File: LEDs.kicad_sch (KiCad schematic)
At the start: 13 parts

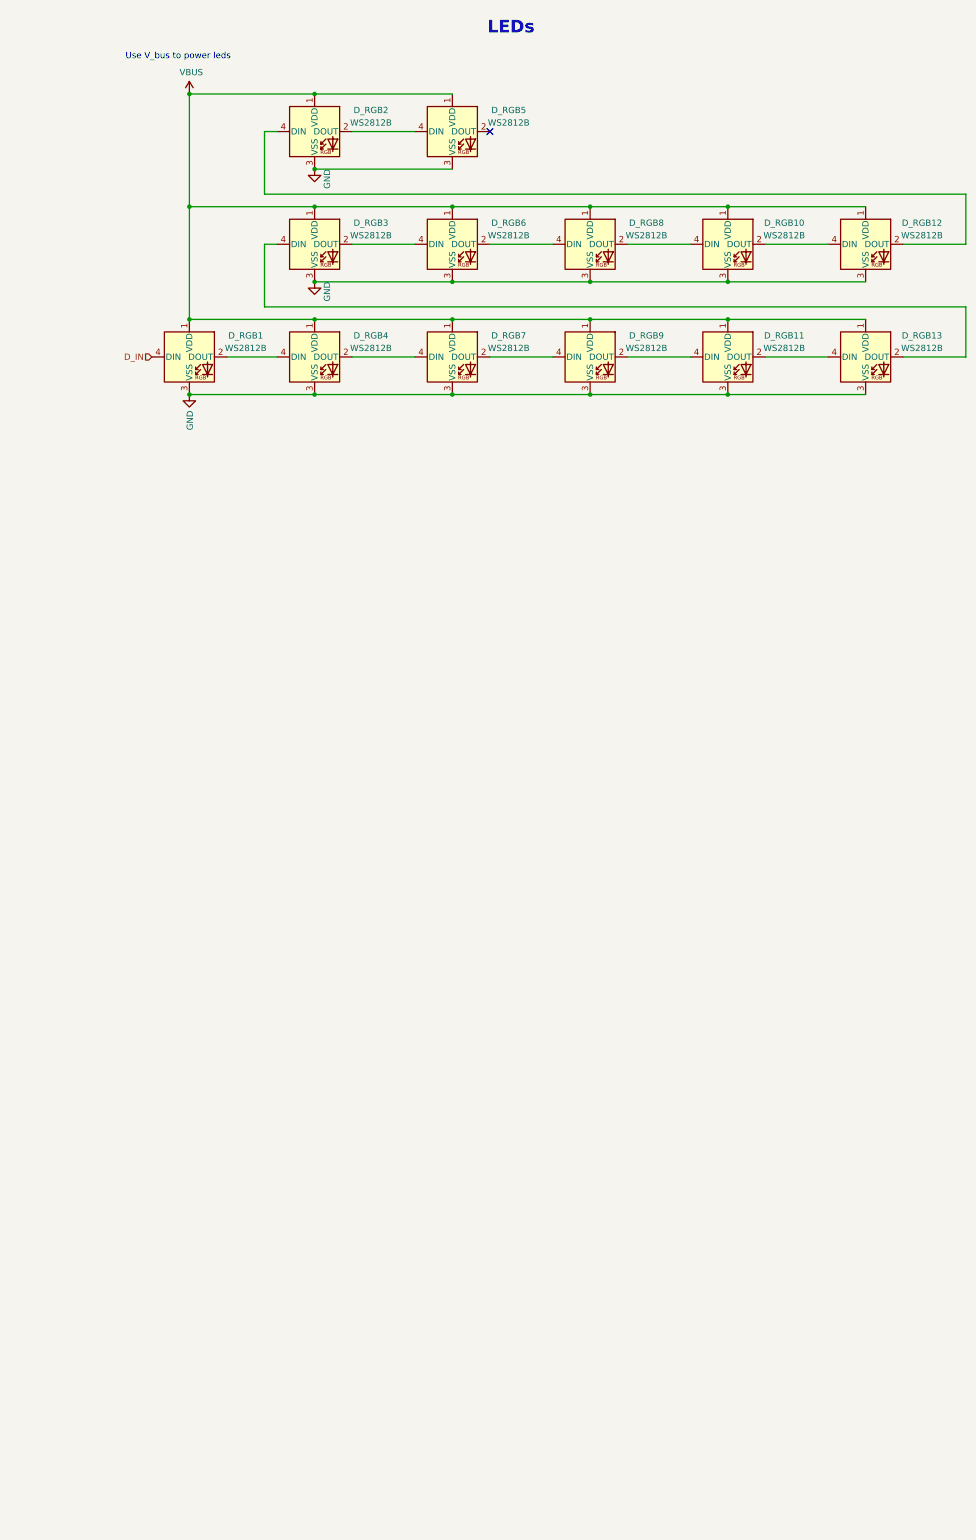
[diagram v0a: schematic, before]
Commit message: per key rgb (reverse mount sk6812 mini e, geometry finalisation
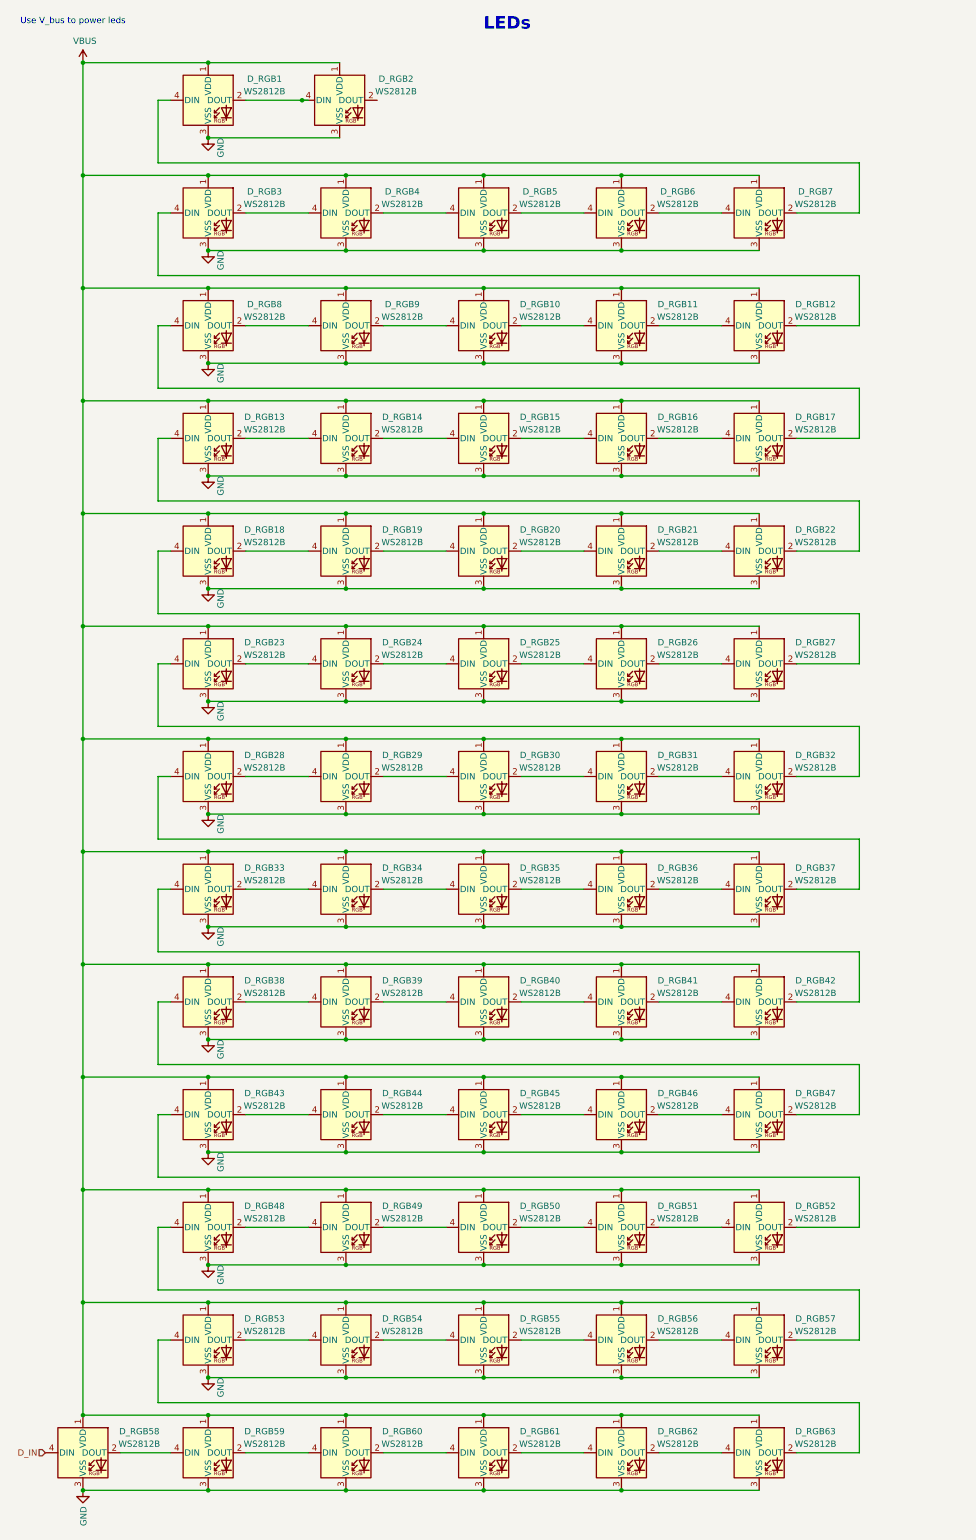
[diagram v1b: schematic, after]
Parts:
- added D_RGB1, D_RGB10, D_RGB11, D_RGB12, D_RGB13, D_RGB14, D_RGB15, D_RGB16, D_RGB17, D_RGB18, D_RGB19, D_RGB20, D_RGB21, D_RGB22, D_RGB23, D_RGB24, D_RGB25, D_RGB26, D_RGB27, D_RGB28, D_RGB29, D_RGB3, D_RGB30, D_RGB31, D_RGB32, D_RGB33, D_RGB34, D_RGB35, D_RGB36, D_RGB37, D_RGB38, D_RGB39, D_RGB4, D_RGB40, D_RGB41, D_RGB42, D_RGB43, D_RGB44, D_RGB45, D_RGB46, D_RGB47, D_RGB48, D_RGB49, D_RGB50, D_RGB51, D_RGB52, D_RGB6, D_RGB7, D_RGB8, D_RGB9: WS2812B, kbd:LED_SK6812MINI_E_3.5x3.5mm_P1.75mm, symbol LED:WS2812B
- D_RGB2, D_RGB5: footprint LED_SMD:LED_WS2812B_PLCC4_5.0x5.0mm_P3.2mm -> kbd:LED_SK6812MINI_E_3.5x3.5mm_P1.75mm
- D_RGB53: renamed from D_RGB3; footprint LED_SMD:LED_WS2812B_PLCC4_5.0x5.0mm_P3.2mm -> kbd:LED_SK6812MINI_E_3.5x3.5mm_P1.75mm
- D_RGB54: renamed from D_RGB6; footprint LED_SMD:LED_WS2812B_PLCC4_5.0x5.0mm_P3.2mm -> kbd:LED_SK6812MINI_E_3.5x3.5mm_P1.75mm
- D_RGB55: renamed from D_RGB8; footprint LED_SMD:LED_WS2812B_PLCC4_5.0x5.0mm_P3.2mm -> kbd:LED_SK6812MINI_E_3.5x3.5mm_P1.75mm
- D_RGB56: renamed from D_RGB10; footprint LED_SMD:LED_WS2812B_PLCC4_5.0x5.0mm_P3.2mm -> kbd:LED_SK6812MINI_E_3.5x3.5mm_P1.75mm
- D_RGB57: renamed from D_RGB12; footprint LED_SMD:LED_WS2812B_PLCC4_5.0x5.0mm_P3.2mm -> kbd:LED_SK6812MINI_E_3.5x3.5mm_P1.75mm
- D_RGB58: renamed from D_RGB1; footprint Connector_JST:JST_XH_B5B-XH-A_1x05_P2.50mm_Vertical -> kbd:LED_SK6812MINI_E_3.5x3.5mm_P1.75mm
- D_RGB59: renamed from D_RGB4; footprint LED_SMD:LED_WS2812B_PLCC4_5.0x5.0mm_P3.2mm -> kbd:LED_SK6812MINI_E_3.5x3.5mm_P1.75mm
- D_RGB60: renamed from D_RGB7; footprint LED_SMD:LED_WS2812B_PLCC4_5.0x5.0mm_P3.2mm -> kbd:LED_SK6812MINI_E_3.5x3.5mm_P1.75mm
- D_RGB61: renamed from D_RGB9; footprint LED_SMD:LED_WS2812B_PLCC4_5.0x5.0mm_P3.2mm -> kbd:LED_SK6812MINI_E_3.5x3.5mm_P1.75mm
- D_RGB62: renamed from D_RGB11; footprint LED_SMD:LED_WS2812B_PLCC4_5.0x5.0mm_P3.2mm -> kbd:LED_SK6812MINI_E_3.5x3.5mm_P1.75mm
- D_RGB63: renamed from D_RGB13; footprint LED_SMD:LED_WS2812B_PLCC4_5.0x5.0mm_P3.2mm -> kbd:LED_SK6812MINI_E_3.5x3.5mm_P1.75mm
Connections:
- net GND: now also D_RGB1.3 (VSS), D_RGB10.3 (VSS), D_RGB11.3 (VSS), D_RGB12.3 (VSS), D_RGB13.3 (VSS), D_RGB14.3 (VSS), D_RGB15.3 (VSS), D_RGB16.3 (VSS), D_RGB17.3 (VSS), D_RGB18.3 (VSS), D_RGB19.3 (VSS), D_RGB20.3 (VSS), D_RGB21.3 (VSS), D_RGB22.3 (VSS), D_RGB23.3 (VSS), D_RGB24.3 (VSS), D_RGB25.3 (VSS), D_RGB26.3 (VSS), D_RGB27.3 (VSS), D_RGB28.3 (VSS), D_RGB29.3 (VSS), D_RGB3.3 (VSS), D_RGB30.3 (VSS), D_RGB31.3 (VSS), D_RGB32.3 (VSS), D_RGB33.3 (VSS), D_RGB34.3 (VSS), D_RGB35.3 (VSS), D_RGB36.3 (VSS), D_RGB37.3 (VSS), D_RGB38.3 (VSS), D_RGB39.3 (VSS), D_RGB4.3 (VSS), D_RGB40.3 (VSS), D_RGB41.3 (VSS), D_RGB42.3 (VSS), D_RGB43.3 (VSS), D_RGB44.3 (VSS), D_RGB45.3 (VSS), D_RGB46.3 (VSS), D_RGB47.3 (VSS), D_RGB48.3 (VSS), D_RGB49.3 (VSS), D_RGB50.3 (VSS), D_RGB51.3 (VSS), D_RGB52.3 (VSS), D_RGB6.3 (VSS), D_RGB7.3 (VSS), D_RGB8.3 (VSS), D_RGB9.3 (VSS)
- net VBUS: now also D_RGB1.1 (VDD), D_RGB10.1 (VDD), D_RGB11.1 (VDD), D_RGB12.1 (VDD), D_RGB13.1 (VDD), D_RGB14.1 (VDD), D_RGB15.1 (VDD), D_RGB16.1 (VDD), D_RGB17.1 (VDD), D_RGB18.1 (VDD), D_RGB19.1 (VDD), D_RGB20.1 (VDD), D_RGB21.1 (VDD), D_RGB22.1 (VDD), D_RGB23.1 (VDD), D_RGB24.1 (VDD), D_RGB25.1 (VDD), D_RGB26.1 (VDD), D_RGB27.1 (VDD), D_RGB28.1 (VDD), D_RGB29.1 (VDD), D_RGB3.1 (VDD), D_RGB30.1 (VDD), D_RGB31.1 (VDD), D_RGB32.1 (VDD), D_RGB33.1 (VDD), D_RGB34.1 (VDD), D_RGB35.1 (VDD), D_RGB36.1 (VDD), D_RGB37.1 (VDD), D_RGB38.1 (VDD), D_RGB39.1 (VDD), D_RGB4.1 (VDD), D_RGB40.1 (VDD), D_RGB41.1 (VDD), D_RGB42.1 (VDD), D_RGB43.1 (VDD), D_RGB44.1 (VDD), D_RGB45.1 (VDD), D_RGB46.1 (VDD), D_RGB47.1 (VDD), D_RGB48.1 (VDD), D_RGB49.1 (VDD), D_RGB50.1 (VDD), D_RGB51.1 (VDD), D_RGB52.1 (VDD), D_RGB6.1 (VDD), D_RGB7.1 (VDD), D_RGB8.1 (VDD), D_RGB9.1 (VDD)
- net at D_RGB2.4 (DIN): now also D_RGB1.2 (DOUT); no longer D_RGB57.2 (DOUT)
- net at D_RGB5.4 (DIN): now also D_RGB4.2 (DOUT); no longer D_RGB2.2 (DOUT)
- net at D_RGB5.2 (DOUT): now also D_RGB6.4 (DIN)
- new net: D_RGB13.2 (DOUT), D_RGB14.4 (DIN)
- new net: D_RGB13.4 (DIN), D_RGB22.2 (DOUT)
- new net: D_RGB18.2 (DOUT), D_RGB19.4 (DIN)
- new net: D_RGB18.4 (DIN), D_RGB27.2 (DOUT)
- new net: D_RGB51.2 (DOUT), D_RGB52.4 (DIN)
- new net: D_RGB50.2 (DOUT), D_RGB51.4 (DIN)
- new net: D_RGB44.2 (DOUT), D_RGB45.4 (DIN)
- new net: D_RGB43.2 (DOUT), D_RGB44.4 (DIN)
- new net: D_RGB41.2 (DOUT), D_RGB42.4 (DIN)
- new net: D_RGB40.2 (DOUT), D_RGB41.4 (DIN)
- new net: D_RGB28.2 (DOUT), D_RGB29.4 (DIN)
- new net: D_RGB28.4 (DIN), D_RGB37.2 (DOUT)
- new net: D_RGB14.2 (DOUT), D_RGB15.4 (DIN)
- new net: D_RGB33.2 (DOUT), D_RGB34.4 (DIN)
- new net: D_RGB33.4 (DIN), D_RGB42.2 (DOUT)
- new net: D_RGB3.2 (DOUT), D_RGB4.4 (DIN)
- new net: D_RGB31.2 (DOUT), D_RGB32.4 (DIN)
- new net: D_RGB30.2 (DOUT), D_RGB31.4 (DIN)
- new net: D_RGB16.2 (DOUT), D_RGB17.4 (DIN)
- new net: D_RGB15.2 (DOUT), D_RGB16.4 (DIN)
- new net: D_RGB10.2 (DOUT), D_RGB11.4 (DIN)
- new net: D_RGB10.4 (DIN), D_RGB9.2 (DOUT)
- new net: D_RGB11.2 (DOUT), D_RGB12.4 (DIN)
- new net: D_RGB45.2 (DOUT), D_RGB46.4 (DIN)
- new net: D_RGB36.2 (DOUT), D_RGB37.4 (DIN)
- new net: D_RGB46.2 (DOUT), D_RGB47.4 (DIN)
- new net: D_RGB23.2 (DOUT), D_RGB24.4 (DIN)
- new net: D_RGB23.4 (DIN), D_RGB32.2 (DOUT)
- new net: D_RGB8.2 (DOUT), D_RGB9.4 (DIN)
- new net: D_RGB17.2 (DOUT), D_RGB8.4 (DIN)
- new net: D_RGB43.4 (DIN), D_RGB52.2 (DOUT)
- new net: D_RGB38.2 (DOUT), D_RGB39.4 (DIN)
- new net: D_RGB38.4 (DIN), D_RGB47.2 (DOUT)
- new net: D_RGB39.2 (DOUT), D_RGB40.4 (DIN)
- new net: D_RGB48.2 (DOUT), D_RGB49.4 (DIN)
- new net: D_RGB48.4 (DIN), D_RGB57.2 (DOUT)
- new net: D_RGB24.2 (DOUT), D_RGB25.4 (DIN)
- new net: D_RGB26.2 (DOUT), D_RGB27.4 (DIN)
- new net: D_RGB25.2 (DOUT), D_RGB26.4 (DIN)
- new net: D_RGB35.2 (DOUT), D_RGB36.4 (DIN)
- new net: D_RGB12.2 (DOUT), D_RGB3.4 (DIN)
- new net: D_RGB1.4 (DIN), D_RGB7.2 (DOUT)
- new net: D_RGB34.2 (DOUT), D_RGB35.4 (DIN)
- new net: D_RGB6.2 (DOUT), D_RGB7.4 (DIN)
- new net: D_RGB29.2 (DOUT), D_RGB30.4 (DIN)
- new net: D_RGB19.2 (DOUT), D_RGB20.4 (DIN)
- new net: D_RGB20.2 (DOUT), D_RGB21.4 (DIN)
- new net: D_RGB21.2 (DOUT), D_RGB22.4 (DIN)
- new net: D_RGB49.2 (DOUT), D_RGB50.4 (DIN)
- no-connect marks 1 -> 0
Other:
- moved on the sheet: D_RGB53, D_RGB54, D_RGB55, D_RGB56, D_RGB57, D_RGB58, D_RGB59, D_RGB60, D_RGB61, D_RGB62, D_RGB63

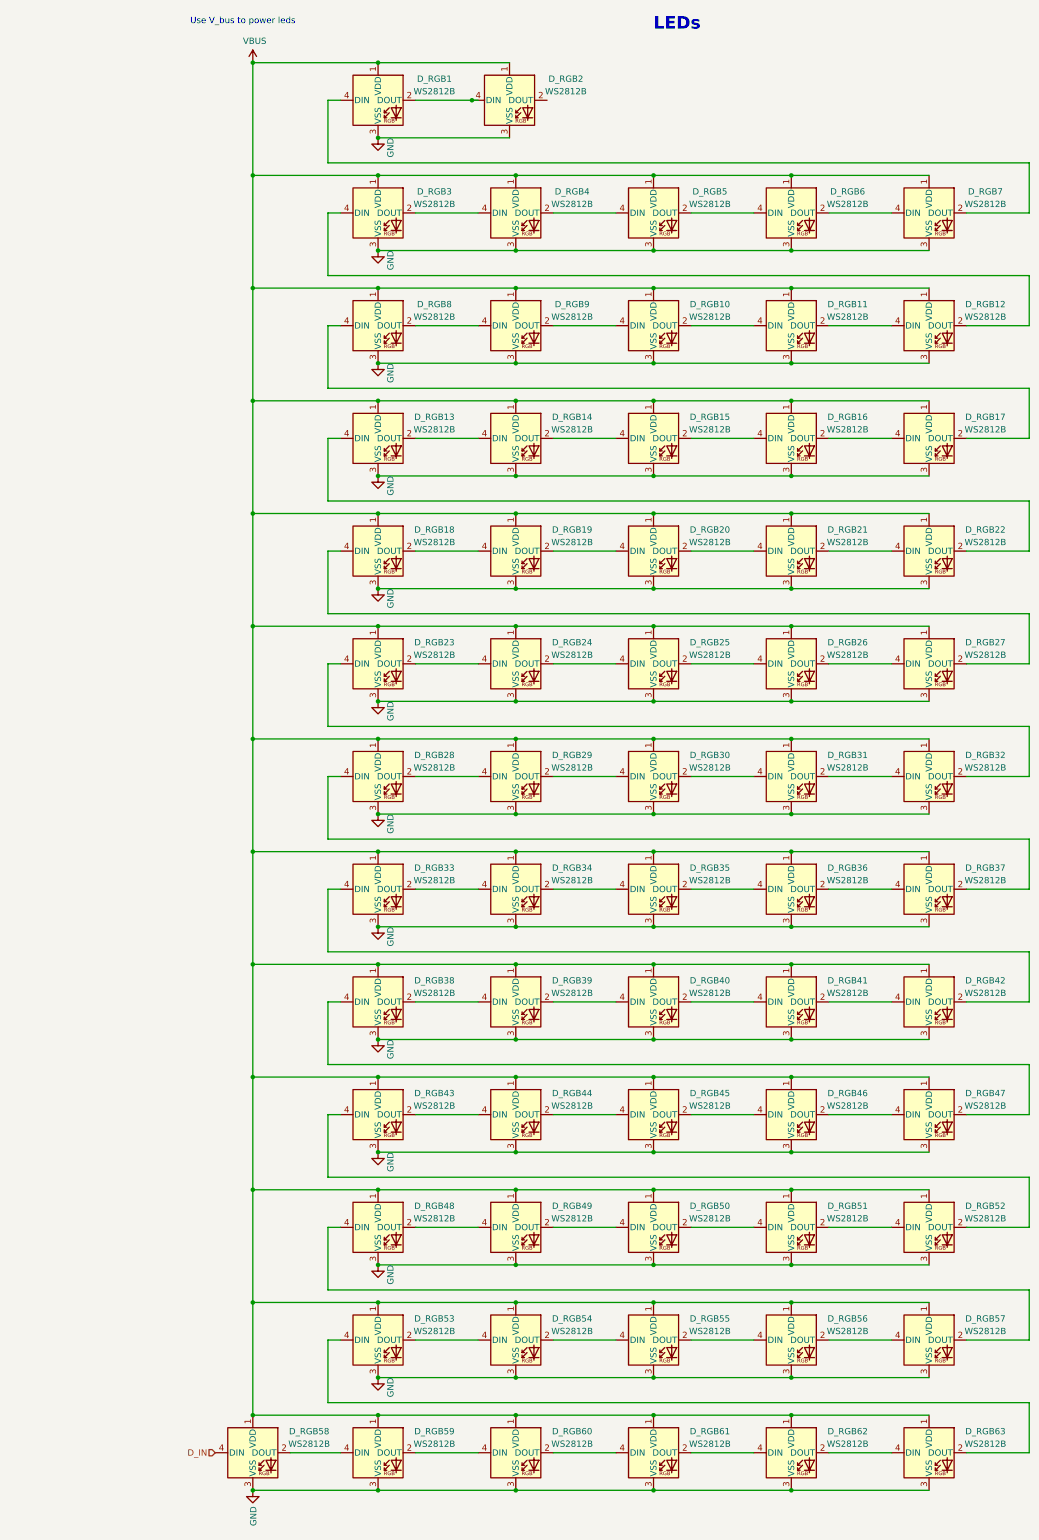
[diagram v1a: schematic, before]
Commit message: remove left most column, reroute rp2040
remove left most column, reroute rp2040 to fit in-between switches, no more oled, last 2 cols (right) are snap off. 
still to do:
- check that the snap cutouts aren't too much,
- add mounting holes for if the side is snapped off.
- still to route columns/rows
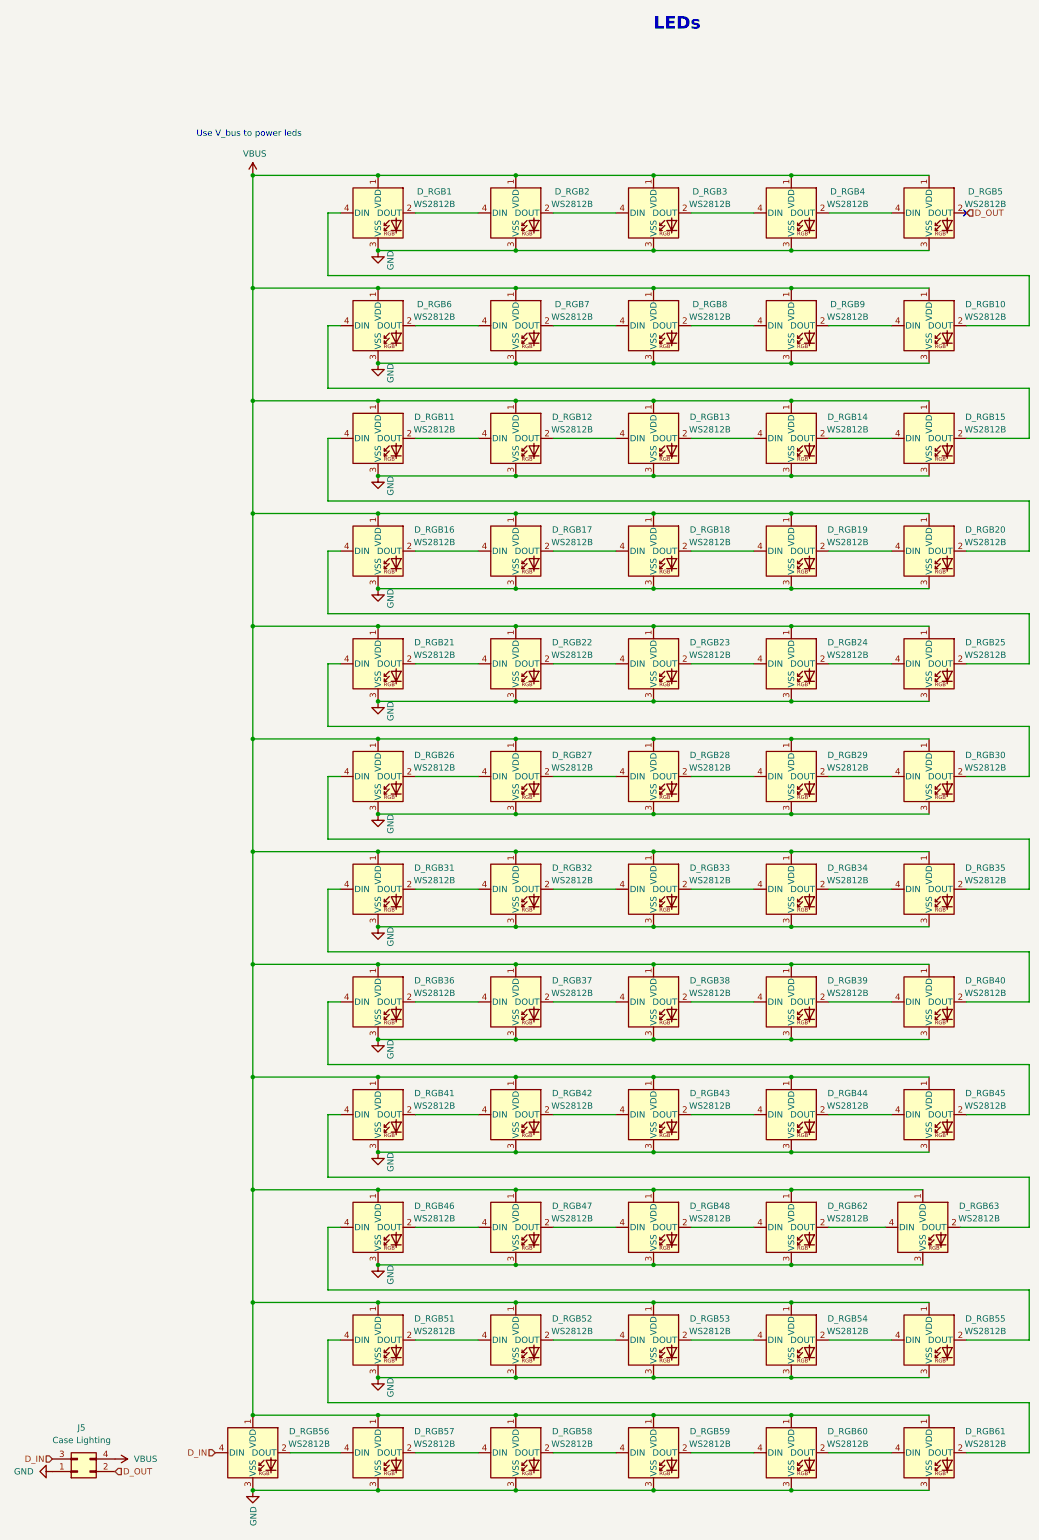
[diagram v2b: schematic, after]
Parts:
- removed D_RGB1, D_RGB2, D_RGB49, D_RGB50, D_RGB52: WS2812B, kbd:LED_SK6812MINI_E_3.5x3.5mm_P1.75mm, symbol LED:WS2812B
- added D_RGB47, D_RGB48, D_RGB63: WS2812B, kbd:LED_SK6812MINI_E_3.5x3.5mm_P1.75mm, symbol LED:WS2812B
- added J5: Case Lighting, Connector_JST:JST_PH_S4B-PH-K_1x04_P2.00mm_Horizontal, symbol Connector_Generic:Conn_02x02_Odd_Even
- renumbered D_RGB3 to D_RGB1, D_RGB12 to D_RGB10, D_RGB13 to D_RGB11, D_RGB14 to D_RGB12, D_RGB15 to D_RGB13, D_RGB16 to D_RGB14, D_RGB17 to D_RGB15, D_RGB18 to D_RGB16, D_RGB19 to D_RGB17, D_RGB20 to D_RGB18, D_RGB21 to D_RGB19, D_RGB4 to D_RGB2, D_RGB22 to D_RGB20, D_RGB23 to D_RGB21, D_RGB24 to D_RGB22, D_RGB25 to D_RGB23, D_RGB26 to D_RGB24, D_RGB27 to D_RGB25, D_RGB28 to D_RGB26, D_RGB29 to D_RGB27, D_RGB30 to D_RGB28, D_RGB31 to D_RGB29, D_RGB5 to D_RGB3, D_RGB32 to D_RGB30, D_RGB33 to D_RGB31, D_RGB34 to D_RGB32, D_RGB35 to D_RGB33, D_RGB36 to D_RGB34, D_RGB37 to D_RGB35, D_RGB38 to D_RGB36, D_RGB39 to D_RGB37, D_RGB40 to D_RGB38, D_RGB41 to D_RGB39, D_RGB6 to D_RGB4, D_RGB42 to D_RGB40, D_RGB43 to D_RGB41, D_RGB44 to D_RGB42, D_RGB45 to D_RGB43, D_RGB46 to D_RGB44, D_RGB47 to D_RGB45, D_RGB48 to D_RGB46, D_RGB7 to D_RGB5, D_RGB53 to D_RGB51, D_RGB54 to D_RGB52, D_RGB55 to D_RGB53, D_RGB56 to D_RGB54, D_RGB57 to D_RGB55, D_RGB58 to D_RGB56, D_RGB59 to D_RGB57, D_RGB60 to D_RGB58, D_RGB61 to D_RGB59, D_RGB8 to D_RGB6, D_RGB62 to D_RGB60, D_RGB63 to D_RGB61, D_RGB51 to D_RGB62, D_RGB9 to D_RGB7, D_RGB10 to D_RGB8, D_RGB11 to D_RGB9
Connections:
- net D_IN: now also J5.3 (Pin_3)
- net GND: now also D_RGB47.3 (VSS), D_RGB48.3 (VSS), D_RGB63.3 (VSS), J5.1 (Pin_1)
- net VBUS: now also D_RGB47.1 (VDD), D_RGB48.1 (VDD), D_RGB63.1 (VDD), J5.4 (Pin_4)
- net at D_RGB62.2 (DOUT): now also D_RGB63.4 (DIN)
- net at D_RGB62.4 (DIN): now also D_RGB48.2 (DOUT)
- net at D_RGB41.4 (DIN): now also D_RGB63.2 (DOUT)
- net at D_RGB46.2 (DOUT): now also D_RGB47.4 (DIN)
- net D_OUT: now reaches D_RGB5.2 (DOUT)
- net D_OUT: now also J5.2 (Pin_2)
- new net: D_RGB47.2 (DOUT), D_RGB48.4 (DIN)
- no-connect marks 0 -> 1
